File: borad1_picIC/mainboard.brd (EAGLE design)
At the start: 42.9 x 44.4 mm, 23 parts, among them IC2 7805TV, K1 G6RW

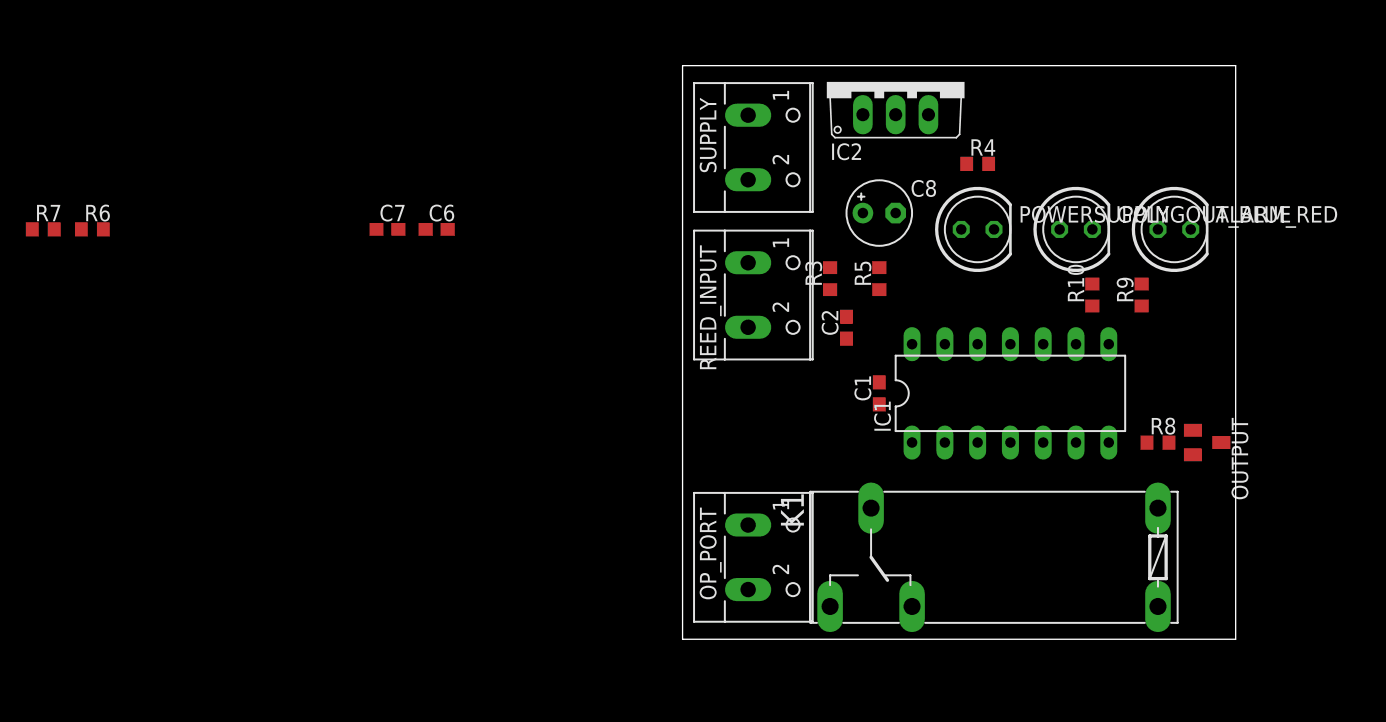
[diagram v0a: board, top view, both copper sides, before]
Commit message: First board ready, just figuring out the placement and connectors.
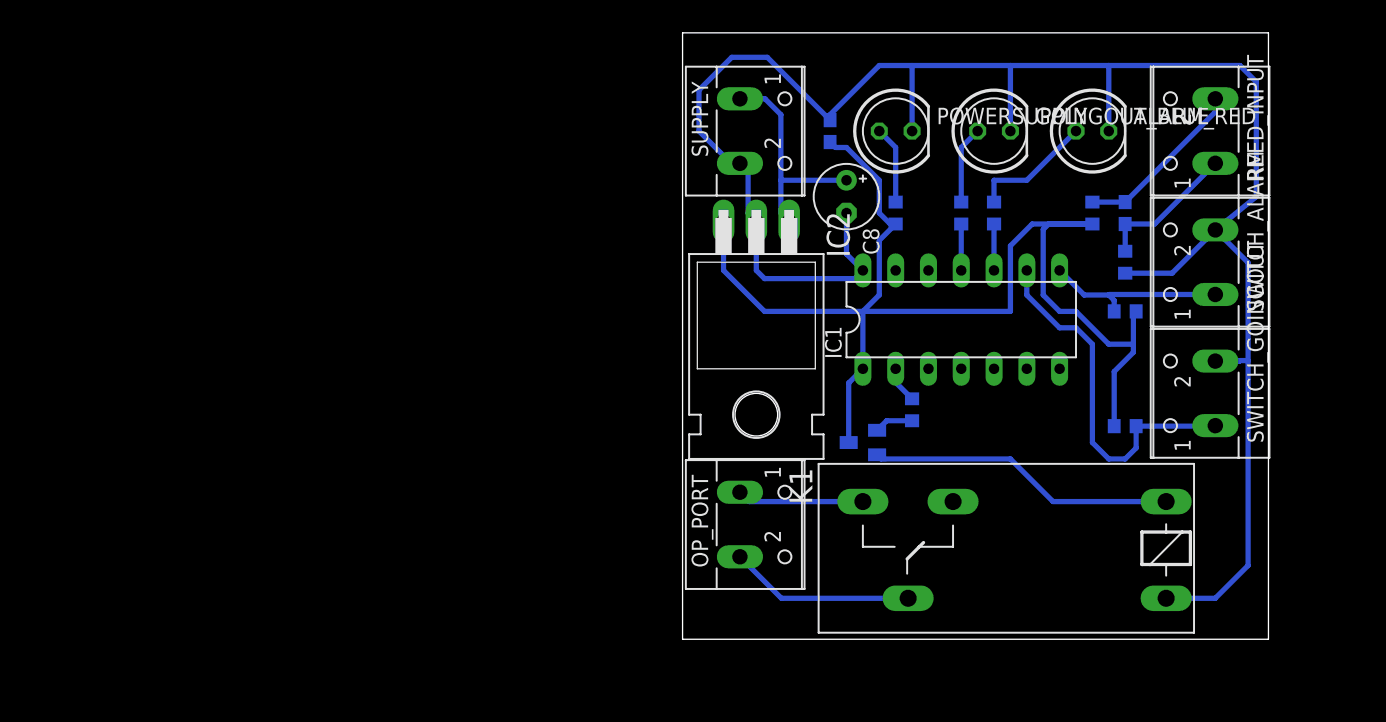
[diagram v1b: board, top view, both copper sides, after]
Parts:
- removed C6, C7: (no value), eagle-ltspice:C0603
- removed R6, R7: (no value), rcl:R0603
- added R1, R2: (no value), rcl:R0603
- added SWITCH_ALARM, SWITCH_GOINGOUT: (no value), con-wago-500:W237-102
- IC2: value 7805TV -> 7805T; device linear:TO220V -> linear:TO220H
- K1: value G6RW -> G2R; device relay:G6RW -> relay:G2R
- moved REED_INPUT 36.0 mm to (40.0, 68.6), turned to 90 degrees
- moved OUTPUT 26.7 mm to (14.0, 44.5), flipped to the bottom
- moved IC2 23.6 mm to (5.71, 51.4), turned to 180 degrees
- moved C2 23.3 mm to (34.3, 62.2), flipped to the bottom, turned to 270 degrees
- moved R3 20.9 mm to (31.8, 62.2), flipped to the bottom, turned to 270 degrees
- moved C1 20.7 mm to (11.4, 68.6), flipped to the bottom
- moved R8 19.2 mm to (17.8, 47.0), flipped to the bottom, turned to 270 degrees
- moved R5 19.1 mm to (34.3, 58.4), flipped to the bottom
- moved R9 13.1 mm to (24.1, 62.2), flipped to the bottom
- moved R10 12.0 mm to (21.6, 62.2), flipped to the bottom
- moved K1 10.8 mm to (34.9, 36.2)
- moved ALARM_RED 9.92 mm to (31.8, 68.6)
- moved GOINGOUT_BLUE 9.92 mm to (24.1, 68.6)
- moved POWERSUPPLY 9.92 mm to (16.5, 68.6)
- moved R4 7.41 mm to (16.5, 62.2), flipped to the bottom, turned to 90 degrees
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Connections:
- new net SWITCH_ALARM: IC1.RC2, R2.1, SWITCH_ALARM.1
- new net SWITCH_GOINGOUT: IC1.RC1, R1.1, SWITCH_GOINGOUT.1
- net ALARM: now also IC1.RC0
- net GND: now also SWITCH_ALARM.2, SWITCH_GOINGOUT.2
- net GOINGOUT: now also IC1.RA2
- net RELAY: now also IC1.RA5
- net VCC: now also R1.2, R2.2
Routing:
- net GND: track 0.00 -> 152.7 mm
- net VCC: track 0.00 -> 94.3 mm
- net SWITCH_GOINGOUT: track 0.00 -> 28.3 mm
- net N$6: track 0.00 -> 23.9 mm
- net N$1: track 0.00 -> 17.3 mm
- net N$8: track 0.00 -> 14.4 mm
- net SWITCH_ALARM: track 0.00 -> 14.3 mm
- net SENSOR: track 0.00 -> 13.4 mm
- net N$7: track 0.00 -> 11.0 mm
- net N$9: track 0.00 -> 9.82 mm
- net N$5: track 0.00 -> 9.62 mm
- net N$3: track 0.00 -> 6.03 mm
- net N$2: track 0.00 -> 6.03 mm
- net GOINGOUT: track 0.00 -> 3.60 mm
- net ALARM: track 0.00 -> 3.60 mm
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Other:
- board size 42.9 x 44.4 mm -> 45.4 x 47 mm

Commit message: Dual layer PCB routed, still needs to be checked from senior
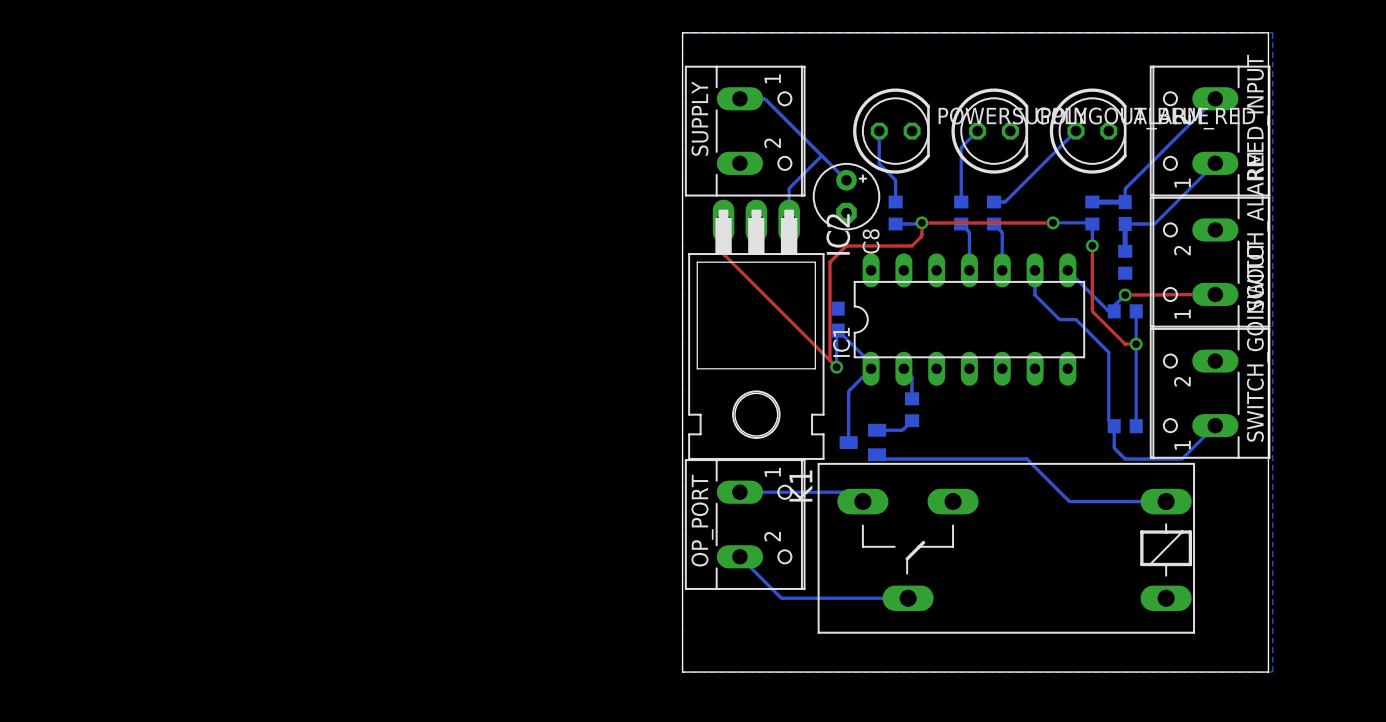
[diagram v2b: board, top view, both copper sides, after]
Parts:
- moved C1 14.6 mm to (12.1, 54.0)
- moved IC1 0.64 mm to (22.2, 54.0)
- turned R1 to 180 degrees
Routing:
- net GND: track 152.7 -> 0.00 mm
- net VCC: track 94.3 -> 80.3 mm, vias 0 -> 5
- net SWITCH_GOINGOUT: track 28.3 -> 26.2 mm
- net N$5: track 9.62 -> 8.61 mm
- net SWITCH_ALARM: track 14.3 -> 13.5 mm, vias 0 -> 1
- added copper zone on layer 16, net GND
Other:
- board size 45.4 x 47 mm -> 45.4 x 49.5 mm

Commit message: Converting everything thing to SMD, All the wires routed, components and connection modified as per suggestion from senior
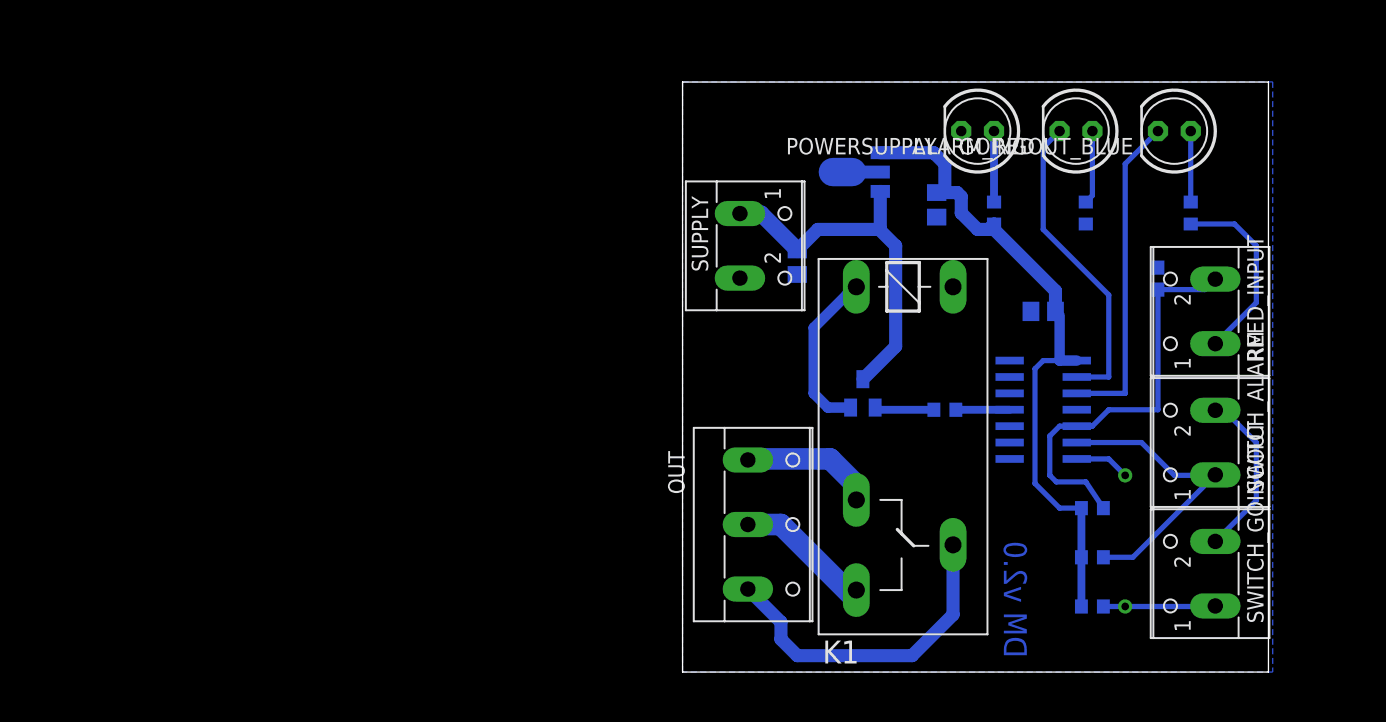
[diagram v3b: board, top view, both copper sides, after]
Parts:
- removed IC1: (no value), pic16f1824_mack:DIL14
- removed OP_PORT: (no value), con-wago-500:W237-102
- removed R5: (no value), rcl:R0603
- added C3: (no value), rcl:C0805
- added OUT: (no value), con-wago-500:W237-103
- added U$1: (no value), microchip-16f688:SOIC14
- C1: value (none) -> 10uF; device eagle-ltspice:C0603 -> rcl:C0805
- C8: value (none) -> 10uF; device rcl:E2,5-5 -> rcl:C0805
- IC2: value 7805T -> 78L05F; device linear:TO220H -> linear:SOT89
- R1, R2, R3: value (none) -> 10k
- R10, R4, R9: value (none) -> 150
- moved K1 25.1 mm to (17.1, 54.0), turned to 270 degrees
- moved R3 22.9 mm to (31.8, 39.4), turned to 0 degrees
- moved R2 19.2 mm to (31.8, 35.6), turned to 0 degrees
- moved R10 17.8 mm to (39.4, 62.2), turned to 270 degrees
- moved IC2 15.9 mm to (13.3, 65.4), flipped to the bottom, turned to 270 degrees
- moved R1 14.2 mm to (31.8, 31.8), turned to 0 degrees
- moved GOINGOUT_BLUE 14.0 mm to (38.1, 68.6), turned to 180 degrees
- moved REED_INPUT 14.0 mm to (40.0, 54.6)
- moved SWITCH_ALARM 14.0 mm to (40.0, 44.5)
- moved SWITCH_GOINGOUT 14.0 mm to (40.0, 34.3)
- moved C1 11.7 mm to (19.7, 62.9), turned to 270 degrees
- moved SUPPLY 8.89 mm to (5.71, 59.7)
- moved R4 7.62 mm to (24.1, 62.2)
- moved R9 7.11 mm to (31.2, 62.2), turned to 270 degrees
- moved C8 6.35 mm to (8.89, 58.4), flipped to the bottom
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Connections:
- removed net N$7: C2.2, R5.2, REED_INPUT.1
- new net 12V: C8.1, IC2.3, OUTPUT.3, SUPPLY.1
- net ALARM: now also ALARM_RED.K, U$1.2; no longer IC1.RC0, R9.1
- net GND: now also C2.2, C3.2, C8.2, IC2.2@1, R10.2, R9.2, REED_INPUT.1, U$1.14; no longer ALARM_RED.K, C8.-, GOINGOUT_BLUE.K, IC1.VSS, R5.1
- net GOINGOUT: now also GOINGOUT_BLUE.K, U$1.3; no longer IC1.RA2, R10.1
- net N$1: now also K1.O, OUT.1; no longer C8.+, IC2.1, SUPPLY.1
- net N$2: now also R10.1; no longer R10.2
- net N$5: now also R9.1; no longer R9.2
- net N$8: now also OUT.3; no longer OP_PORT.2
- net N$9: now also OUT.2; no longer OP_PORT.1
- net RELAY: now also U$1.11; no longer IC1.RA5
- net SENSOR: now also U$1.5
- net SWITCH_ALARM: now also U$1.6; no longer IC1.RC2
- net SWITCH_GOINGOUT: now also U$1.7; no longer IC1.RC1
- net VCC: now also C3.1, IC2.1, U$1.1; no longer IC1.VDD, IC2.3, OUTPUT.3
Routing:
- net 12V: track 0.00 -> 28.8 mm
- net GND: track 0.00 -> 27.9 mm
- net VCC: track 80.3 -> 52.9 mm, vias 5 -> 0
- net GOINGOUT: track 3.84 -> 25.1 mm
- net ALARM: track 3.84 -> 24.2 mm
- net SENSOR: track 13.4 -> 31.8 mm
- net SWITCH_GOINGOUT: track 26.2 -> 13.0 mm, vias 0 -> 1
- net N$8: track 14.3 -> 25.5 mm
- net N$7: track 11.0 -> 0.00 mm, vias 0 -> 1
- net N$6: track 23.9 -> 13.0 mm
- net SWITCH_ALARM: track 13.5 -> 23.1 mm, vias 1 -> 0
- net N$1: track 17.0 -> 10.4 mm
- net N$5: track 8.61 -> 5.71 mm
- net N$4: track 3.00 -> 4.62 mm
- net RELAY: track 2.57 -> 4.17 mm
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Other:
- board size 45.4 x 49.5 mm -> 45.4 x 45.7 mm
- board text added: "DM v2.0"

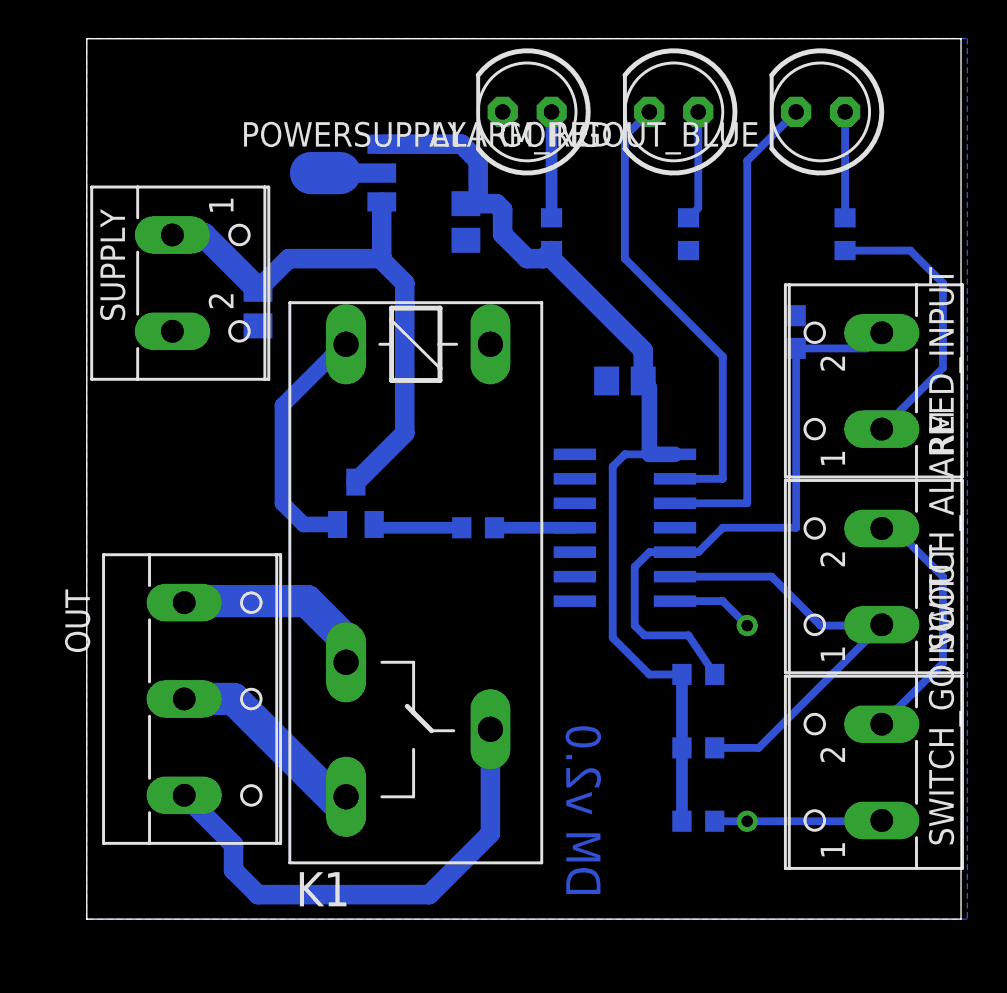
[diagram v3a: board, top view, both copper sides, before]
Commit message: Changing Relay foot print to available relay and rerouted the whole PCB
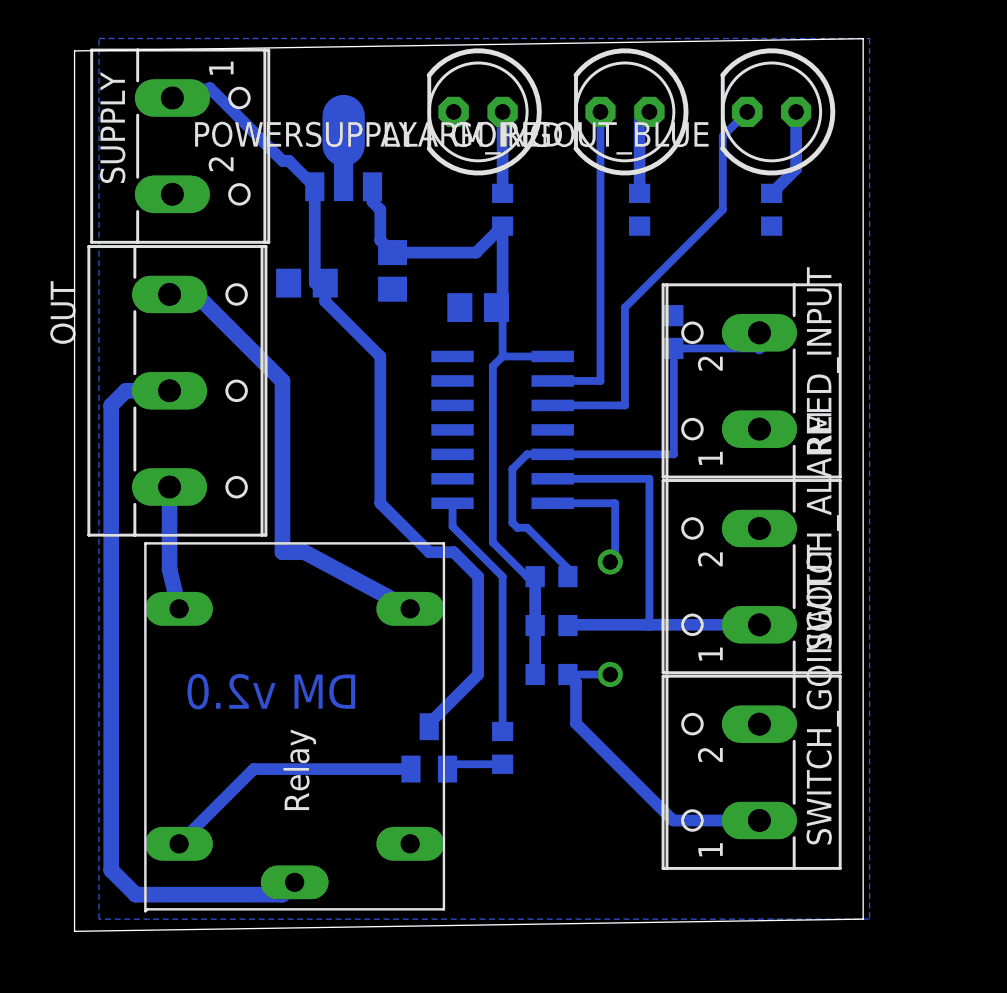
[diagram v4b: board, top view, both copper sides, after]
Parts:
- removed K1: G2R, relay:G2R
- added U$2: (no value), JQC-3FC_relay:JQC-3FC
- moved OUT 16.0 mm to (5.59, 54.1)
- moved OUTPUT 13.3 mm to (17.8, 35.6)
- moved R8 11.5 mm to (21.6, 35.6), turned to 270 degrees
- moved R1 10.8 mm to (24.1, 39.4)
- moved R2 9.92 mm to (24.1, 41.9)
- moved R3 9.16 mm to (24.1, 44.5)
- moved C3 8.52 mm to (20.3, 58.4)
- moved U$1 8.13 mm to (21.6, 52.1)
- moved SUPPLY 7.11 mm to (5.71, 66.8)
- moved REED_INPUT 6.35 mm to (33.7, 54.6)
- moved SWITCH_ALARM 6.35 mm to (33.7, 44.5)
- moved SWITCH_GOINGOUT 6.35 mm to (33.7, 34.3)
- moved C2 6.35 mm to (30.5, 57.1)
- moved C1 4.58 mm to (15.9, 60.3)
- moved R10 4.02 mm to (35.6, 63.5)
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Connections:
- net GND: now also U$2.COIL_2; no longer K1.2
- net N$1: now also OUTPUT.2, U$2.COIL_1; no longer K1.O, OUT.1
- net N$6: now also OUT.1, U$2.NC; no longer K1.1, OUTPUT.2
- net N$8: now also U$2.NO; no longer K1.P
- net N$9: now also U$2.COMM; no longer K1.S
- net RELAY: now also U$1.8; no longer U$1.11
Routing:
- net GND: track 27.9 -> 0.00 mm
- net N$9: track 11.6 -> 37.8 mm
- net N$8: track 25.5 -> 6.38 mm
- net VCC: track 52.9 -> 37.6 mm
- net 12V: track 28.8 -> 43.2 mm
- net N$6: track 13.0 -> 24.0 mm
- net SWITCH_GOINGOUT: track 13.0 -> 22.9 mm
- net RELAY: track 4.17 -> 12.9 mm
- net ALARM: track 24.2 -> 16.4 mm
- net SENSOR: track 31.8 -> 26.5 mm
- net GOINGOUT: track 25.1 -> 21.6 mm
- net N$1: track 10.4 -> 13.6 mm
- net N$4: track 4.62 -> 2.96 mm
- net N$3: track 5.50 -> 4.23 mm
- net N$5: track 5.71 -> 4.44 mm
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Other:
- board size 45.4 x 45.7 mm -> 40.9 x 46.3 mm
